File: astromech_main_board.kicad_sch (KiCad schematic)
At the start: 76 parts, among them IC1 MAX11645EUA+, J10 Conn_01x05, J11 Conn_01x06, J13 Conn_01x05, J14 Conn_01x04, J15 Conn_01x04, J18 Screw_Terminal_01x10, J19 Conn_01x04, J2 Conn_02x03_Odd_Even, J20 Conn_01x04, J21 Conn_01x04, J4 IO_XPAND, J5 Conn_01x06, J6 Conn_01x06, J8 Conn_01x03, J9 Conn_01x06, Q1 2N7002, U10 LS7366R, U11 LS7366R, U3 NCP1117-3.3_SOT223, U4 NCP1117-5.0_TO252, U5 SC16IS752IPW_128, U6 PCF8575PWR, U7 TCA9517ADGK, U8 74HC14, U9 LS7366R, Y1 8MHz, Y2 Crystal

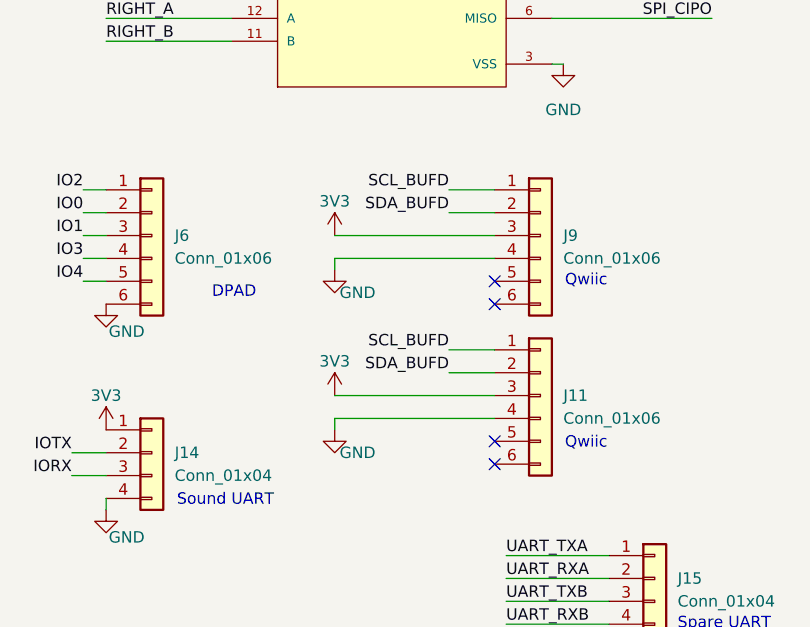
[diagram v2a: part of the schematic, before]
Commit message: switch qwiic pinout order
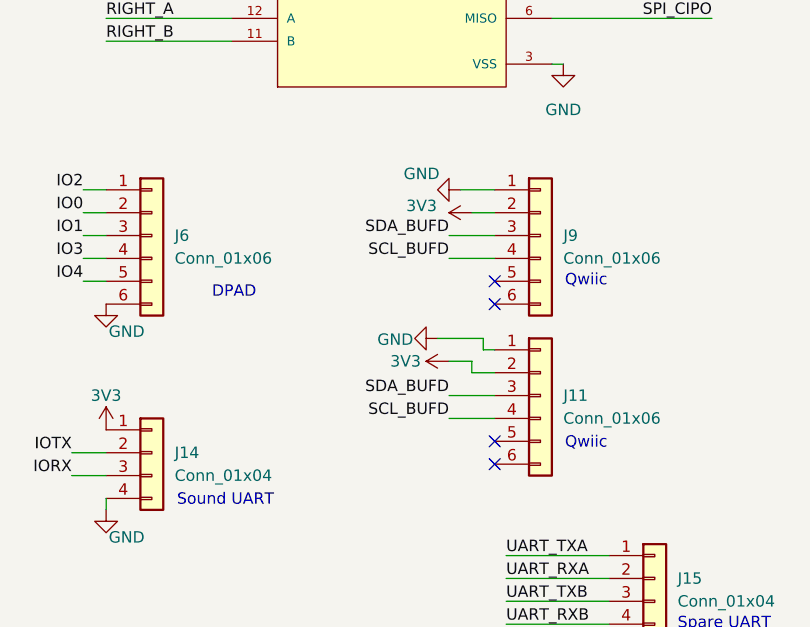
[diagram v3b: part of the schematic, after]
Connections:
- net 3V3: now also J11.2 (Pin_2), J9.2 (Pin_2); no longer J11.3 (Pin_3), J9.3 (Pin_3)
- net GND: now also J11.1 (Pin_1), J9.1 (Pin_1); no longer J11.4 (Pin_4), J9.4 (Pin_4)
- net SCL_BUFD: now also J11.4 (Pin_4), J9.4 (Pin_4); no longer J11.1 (Pin_1), J9.1 (Pin_1)
- net SDA_BUFD: now also J11.3 (Pin_3), J9.3 (Pin_3); no longer J11.2 (Pin_2), J9.2 (Pin_2)
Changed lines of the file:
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@@
 	(wire
 		(pts
-			(xy 257.81 182.88) (xy 252.73 182.88)
+			(xy 257.81 185.42) (xy 252.73 185.42)
 		)
 		(stroke
@@
 	(wire
 		(pts
+			(xy 252.73 203.2) (xy 257.81 203.2)
+		)
+		(stroke
+			(width 0)
+			(type default)
+		)
+	)
+	(wire
+		(pts
 			(xy -66.04 80.01) (xy -80.01 80.01)
 		)
@@
 	(wire
 		(pts
-			(xy 240.03 205.74) (xy 240.03 207.01)
+			(xy 251.46 196.85) (xy 256.54 196.85)
 		)
 		(stroke
@@
 		)
 	)
-	(wire
-		(pts
-			(xy 240.03 205.74) (xy 257.81 205.74)
-		)
-		(stroke
-			(width 0)
-			(type default)
-		)
-	)
 	(polyline
 		(pts
@@
 	(wire
 		(pts
-			(xy 252.73 198.12) (xy 257.81 198.12)
-		)
-		(stroke
-			(width 0)
-			(type default)
-		)
-	)
-	(wire
-		(pts
 			(xy 63.5 31.75) (xy 63.5 35.56)
 		)
@@
 		)
 	)
+	(wire
+		(pts
+			(xy 257.81 200.66) (xy 255.27 200.66)
+		)
+		(stroke
+			(width 0)
+			(type default)
+		)
+	)
 	(polyline
 		(pts
@@
 	(wire
 		(pts
-			(xy 240.03 187.96) (xy 257.81 187.96)
+			(xy 181.61 212.09) (xy 185.42 212.09)
 		)
 		(stroke
@@
 	(wire
 		(pts
-			(xy 181.61 212.09) (xy 185.42 212.09)
+			(xy 264.16 106.68) (xy 281.94 106.68)
 		)
 		(stroke
@@
 	(wire
 		(pts
-			(xy 264.16 106.68) (xy 281.94 106.68)
+			(xy 91.44 64.77) (xy 85.09 64.77)
 		)
 		(stroke
@@
 	(wire
 		(pts
-			(xy 91.44 64.77) (xy 85.09 64.77)
+			(xy 24.13 163.83) (xy 26.67 163.83)
 		)
 		(stroke
@@
 	(wire
 		(pts
-			(xy 24.13 163.83) (xy 26.67 163.83)
+			(xy 198.12 90.17) (xy 200.66 90.17)
 		)
 		(stroke
@@
 	(wire
 		(pts
-			(xy 198.12 90.17) (xy 200.66 90.17)
+			(xy 256.54 198.12) (xy 256.54 196.85)
 		)
 		(stroke
@@
 	(wire
 		(pts
-			(xy 252.73 200.66) (xy 257.81 200.66)
-		)
-		(stroke
-			(width 0)
-			(type default)
-		)
-	)
-	(wire
-		(pts
 			(xy 92.71 166.37) (xy 62.23 166.37)
 		)
@@
 	(wire
 		(pts
-			(xy 240.03 187.96) (xy 240.03 189.23)
+			(xy 254 180.34) (xy 257.81 180.34)
 		)
 		(stroke
@@
 	(wire
 		(pts
+			(xy 255.27 200.66) (xy 255.27 199.39)
+		)
+		(stroke
+			(width 0)
+			(type default)
+		)
+	)
+	(wire
+		(pts
 			(xy 83.82 267.97) (xy 90.17 267.97)
 		)
@@
 	(wire
 		(pts
-			(xy 257.81 180.34) (xy 252.73 180.34)
+			(xy 257.81 187.96) (xy 252.73 187.96)
 		)
 		(stroke
@@
 	(wire
 		(pts
-			(xy 240.03 203.2) (xy 257.81 203.2)
+			(xy 252.73 205.74) (xy 257.81 205.74)
 		)
 		(stroke
@@
 	(wire
 		(pts
+			(xy 255.27 182.88) (xy 257.81 182.88)
+		)
+		(stroke
+			(width 0)
+			(type default)
+		)
+	)
+	(wire
+		(pts
 			(xy 86.36 86.36) (xy 85.09 86.36)
 		)
@@
 	(wire
 		(pts
-			(xy 240.03 185.42) (xy 257.81 185.42)
-		)
-		(stroke
-			(width 0)
-			(type default)
-		)
-	)
-	(wire
-		(pts
 			(xy 100.33 27.94) (xy 100.33 30.48)
 		)
@@
 	(wire
 		(pts
+			(xy 257.81 198.12) (xy 256.54 198.12)
+		)
+		(stroke
+			(width 0)
+			(type default)
+		)
+	)
+	(wire
+		(pts
 			(xy 62.23 123.19) (xy 62.23 125.73)
 		)
@@
 	(wire
 		(pts
+			(xy 255.27 199.39) (xy 252.73 199.39)
+		)
+		(stroke
+			(width 0)
+			(type default)
+		)
+	)
+	(wire
+		(pts
 			(xy 180.34 146.05) (xy 203.2 146.05)
 		)
@@
 	)
 	(label "SDA_BUFD"
-		(at 252.73 200.66 180)
+		(at 252.73 203.2 180)
 		(effects
 			(font
@@
 	)
 	(label "SCL_BUFD"
-		(at 252.73 180.34 180)
+		(at 252.73 187.96 180)
 		(effects
 			(font
@@
 	)
 	(label "SCL_BUFD"
-		(at 252.73 198.12 180)
+		(at 252.73 205.74 180)
 		(effects
 			(font
@@
 	)
 	(label "SDA_BUFD"
-		(at 252.73 182.88 180)
+		(at 252.73 185.42 180)
 		(effects
 			(font
@@
 	(symbol
 		(lib_id "power:GND")
-		(at 240.03 207.01 0)
+		(at 251.46 196.85 270)
 		(unit 1)
 		(exclude_from_sim no)
@@
 		(dnp no)
 		(property "Reference" "#PWR076"
-			(at 240.03 213.36 0)
+			(at 245.11 196.85 0)
 			(effects
 				(font
@@
 		)
 		(property "Value" "GND"
-			(at 242.57 209.55 0)
+			(at 246.761 196.977 90)
 			(effects
 				(font
@@
 		)
 		(property "Footprint" ""
-			(at 240.03 207.01 0)
+			(at 251.46 196.85 0)
 			(effects
 				(font
@@
 		)
 		(property "Datasheet" ""
-			(at 240.03 207.01 0)
+			(at 251.46 196.85 0)
 			(effects
 				(font
@@
 		)
 		(property "Description" "Power symbol creates a global label with name \"GND\" , ground"
-			(at 240.03 207.01 0)
+			(at 251.46 196.85 0)
 			(effects
 				(font
@@
 	(symbol
 		(lib_id "power:GND")
-		(at 240.03 189.23 0)
+		(at 254 180.34 270)
 		(unit 1)
 		(exclude_from_sim no)
@@
 		(dnp no)
 		(property "Reference" "#PWR078"
-			(at 240.03 195.58 0)
+			(at 247.65 180.34 0)
 			(effects
 				(font
@@
 		)
 		(property "Value" "GND"
-			(at 242.57 191.77 0)
+			(at 249.682 178.562 90)
 			(effects
 				(font
@@
 		)
 		(property "Footprint" ""
-			(at 240.03 189.23 0)
+			(at 254 180.34 0)
 			(effects
 				(font
@@
 		)
 		(property "Datasheet" ""
-			(at 240.03 189.23 0)
+			(at 254 180.34 0)
 			(effects
 				(font
@@
 		)
 		(property "Description" "Power symbol creates a global label with name \"GND\" , ground"
-			(at 240.03 189.23 0)
+			(at 254 180.34 0)
 			(effects
 				(font
@@
 	(symbol
 		(lib_id "power:+3.3V")
-		(at 240.03 203.2 0)
+		(at 252.73 199.39 90)
 		(unit 1)
 		(exclude_from_sim no)
@@
 		(dnp no)
 		(property "Reference" "#PWR075"
-			(at 240.03 207.01 0)
+			(at 256.54 199.39 0)
 			(effects
 				(font
@@
 		)
 		(property "Value" "3V3"
-			(at 240.03 199.39 0)
+			(at 247.904 199.39 90)
 			(effects
 				(font
@@
 		)
 		(property "Footprint" ""
-			(at 240.03 203.2 0)
+			(at 252.73 199.39 0)
 			(effects
 				(font
@@
 		)
 		(property "Datasheet" ""
-			(at 240.03 203.2 0)
+			(at 252.73 199.39 0)
 			(effects
 				(font
@@
 		)
 		(property "Description" "Power symbol creates a global label with name \"+3.3V\""
-			(at 240.03 203.2 0)
+			(at 252.73 199.39 0)
 			(effects
 				(font
@@
 	(symbol
 		(lib_id "power:+3.3V")
-		(at 240.03 185.42 0)
+		(at 255.27 182.88 90)
 		(unit 1)
 		(exclude_from_sim no)
@@
 		(dnp no)
 		(property "Reference" "#PWR077"
-			(at 240.03 189.23 0)
+			(at 259.08 182.88 0)
 			(effects
 				(font
@@
 		)
 		(property "Value" "3V3"
-			(at 240.03 181.61 0)
+			(at 249.682 182.118 90)
 			(effects
 				(font
@@
 		)
 		(property "Footprint" ""
-			(at 240.03 185.42 0)
+			(at 255.27 182.88 0)
 			(effects
 				(font
@@
 		)
 		(property "Datasheet" ""
-			(at 240.03 185.42 0)
+			(at 255.27 182.88 0)
 			(effects
 				(font
@@
 		)
 		(property "Description" "Power symbol creates a global label with name \"+3.3V\""
-			(at 240.03 185.42 0)
+			(at 255.27 182.88 0)
 			(effects
 				(font

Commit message: schematic updates
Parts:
- removed J10, J13: Conn_01x05, astromech_footprints:691210910005, symbol Connector_Generic:Conn_01x05
- removed J14: Conn_01x04, astromech_footprints:691210910004, symbol Connector_Generic:Conn_01x04
- removed J5, J6: Conn_01x06, astromech_footprints:691210910006, symbol Connector_Generic:Conn_01x06
- added J1, J3, J7: Conn_01x03, astromech_footprints:691210910003, symbol Connector_Generic:Conn_01x03
- added J10: 61201621621, astromech_footprints:61201621621, symbol astromech_symbols:6120XX21621_61201621621
- added P15, P16, P17: TestPoint, TestPoint:TestPoint_Pad_D1.0mm, symbol Connector:TestPoint
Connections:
- net 3V3: now also J10.15
- net GND: now also J1.3 (Pin_3), J10.16, J3.3 (Pin_3), J7.3 (Pin_3)
- net IO0: now also J10.12
- net IO1: now also J10.10
- net IO2: now also J10.14
- net IO3: now also J10.8
- net IO38: now also J10.11
- net IO39: now also J10.9
- net IO4: now also J10.6
- net IO8: now also J4.14 (Pin_14); no longer J4.9 (Pin_9)
- net IORX: now also J7.2 (Pin_2)
- net IOTX: now also J7.1 (Pin_1)
- net SCL_BUFD: now also J1.1 (Pin_1), J3.1 (Pin_1)
- net SCR_SPICLK: now also J10.7
- net SCR_SPIQ: now also J10.13
- net SDA_BUFD: now also J1.2 (Pin_2), J3.2 (Pin_2)
- net at U6.13 (P10): now also J4.9 (Pin_9)
- net at U6.14 (P11): now also J4.10 (Pin_10)
- net at U6.15 (P12): now also J4.11 (Pin_11)
- net at U6.16 (P13): now also J4.12 (Pin_12)
- net at U6.17 (P14): now also J4.13 (Pin_13)
- net at U6.18 (P15): now also P15.1
- net at U6.19 (P16): now also P16.1
- net at U6.20 (P17): now also P17.1
- net IO10 renamed TOUCH_X+
- net TOUCH_X+: now also J10.3; no longer J4.10 (Pin_10)
- net IO17 renamed TOUCH_Y+
- net TOUCH_Y+: now also J10.4; no longer J4.11 (Pin_11)
- net IO19 renamed TOUCH_X-
- net TOUCH_X-: now also J10.1; no longer J4.12 (Pin_12)
- net IO21 renamed TOUCH_Y-
- net TOUCH_Y-: now also J10.2; no longer J4.13 (Pin_13)
- net IO35 renamed SCR_D/C
- net SCR_D/C: now also J10.5; no longer J4.14 (Pin_14)
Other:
- note added: "Screen data/command select"
- note added: "Touchscreen"
- moved on the sheet: J8

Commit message: new layout
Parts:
- removed P15, P16, P17: TestPoint, TestPoint:TestPoint_Pad_D1.0mm, symbol Connector:TestPoint
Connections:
- net +3.3V is gone; now on net 3V3: R8.1
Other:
- note added: "Screen/DPAD"
- note removed: "DPAD"
- note removed: "Screen"
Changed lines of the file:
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@@
 	(wire
 		(pts
-			(xy 62.23 186.69) (xy 63.5 186.69)
-		)
-		(stroke
-			(width 0)
-			(type default)
-		)
-	)
-	(wire
-		(pts
 			(xy 144.78 143.51) (xy 144.78 146.05)
 		)
@@
 	(wire
 		(pts
-			(xy 62.23 184.15) (xy 63.5 184.15)
-		)
-		(stroke
-			(width 0)
-			(type default)
-		)
-	)
-	(wire
-		(pts
 			(xy 273.05 93.98) (xy 274.32 93.98)
 		)
@@
 	(wire
 		(pts
-			(xy 63.5 181.61) (xy 62.23 181.61)
-		)
-		(stroke
-			(width 0)
-			(type default)
-		)
-	)
-	(wire
-		(pts
 			(xy 264.16 156.21) (xy 281.94 156.21)
 		)
@@
 		)
 	)
-	(text "DPAD"
-		(exclude_from_sim no)
-		(at 118.872 181.356 0)
-		(effects
-			(font
-				(size 1.27 1.27)
-			)
-		)
-	)
 	(text "Head Motor PWM"
 		(exclude_from_sim no)
@@
 		)
 	)
-	(text "Screen"
+	(text "Screen/DPAD"
 		(exclude_from_sim no)
-		(at 139.192 198.374 0)
+		(at 134.874 197.612 0)
 		(effects
 			(font
@@
 	)
 	(symbol
-		(lib_id "Connector:TestPoint")
-		(at 63.5 181.61 270)
-		(unit 1)
-		(exclude_from_sim no)
-		(in_bom yes)
-		(on_board yes)
-		(dnp no)
-		(property "Reference" "P15"
-			(at 69.85 181.61 90)
-			(effects
-				(font
-					(size 1.27 1.27)
-				)
-			)
-		)
-		(property "Value" "TestPoint"
-			(at 66.802 184.15 90)
-			(effects
-				(font
-					(size 1.27 1.27)
-				)
-				(hide yes)
-			)
-		)
-		(property "Footprint" "TestPoint:TestPoint_Pad_D1.0mm"
-			(at 63.5 186.69 0)
-			(effects
-				(font
-					(size 1.27 1.27)
-				)
-				(hide yes)
-			)
-		)
-		(property "Datasheet" "~"
-			(at 63.5 186.69 0)
-			(effects
-				(font
-					(size 1.27 1.27)
-				)
-				(hide yes)
-			)
-		)
-		(property "Description" "test point"
-			(at 63.5 181.61 0)
-			(effects
-				(font
-					(size 1.27 1.27)
-				)
-				(hide yes)
-			)
-		)
-		(pin "1"
-		)
-		(instances
-			(project "astromech_main_board"
-				(path "/3ed70c37-1dc6-4761-9813-fca49ce12494"
-					(reference "P15")
-					(unit 1)
-				)
-			)
-		)
-	)
-	(symbol
 		(lib_id "power:GND")
 		(at 191.77 92.71 0)
@@
 	)
 	(symbol
-		(lib_id "Connector:TestPoint")
-		(at 63.5 186.69 270)
-		(unit 1)
-		(exclude_from_sim no)
-		(in_bom yes)
-		(on_board yes)
-		(dnp no)
-		(property "Reference" "P17"
-			(at 69.85 186.69 90)
-			(effects
-				(font
-					(size 1.27 1.27)
-				)
-			)
-		)
-		(property "Value" "TestPoint"
-			(at 66.802 189.23 90)
-			(effects
-				(font
-					(size 1.27 1.27)
-				)
-				(hide yes)
-			)
-		)
-		(property "Footprint" "TestPoint:TestPoint_Pad_D1.0mm"
-			(at 63.5 191.77 0)
-			(effects
-				(font
-					(size 1.27 1.27)
-				)
-				(hide yes)
-			)
-		)
-		(property "Datasheet" "~"
-			(at 63.5 191.77 0)
-			(effects
-				(font
-					(size 1.27 1.27)
-				)
-				(hide yes)
-			)
-		)
-		(property "Description" "test point"
-			(at 63.5 186.69 0)
-			(effects
-				(font
-					(size 1.27 1.27)
-				)
-				(hide yes)
-			)
-		)
-		(pin "1"
-		)
-		(instances
-			(project "astromech_main_board"
-				(path "/3ed70c37-1dc6-4761-9813-fca49ce12494"
-					(reference "P17")
-					(unit 1)
-				)
-			)
-		)
-	)
-	(symbol
 		(lib_id "Connector_Generic:Conn_02x03_Odd_Even")
 		(at 187.96 181.61 0)
@@
 	)
 	(symbol
-		(lib_id "power:+3.3V")
-		(at 175.26 24.13 0)
-		(unit 1)
-		(exclude_from_sim no)
-		(in_bom yes)
-		(on_board yes)
-		(dnp no)
-		(fields_autoplaced yes)
-		(property "Reference" "#PWR09"
-			(at 175.26 27.94 0)
-			(effects
-				(font
-					(size 1.27 1.27)
-				)
-				(hide yes)
-			)
-		)
-		(property "Value" "+3.3V"
-			(at 175.26 19.05 0)
-			(effects
-				(font
-					(size 1.27 1.27)
-				)
-			)
-		)
-		(property "Footprint" ""
-			(at 175.26 24.13 0)
-			(effects
-				(font
-					(size 1.27 1.27)
-				)
-				(hide yes)
-			)
-		)
-		(property "Datasheet" ""
-			(at 175.26 24.13 0)
-			(effects
-				(font
-					(size 1.27 1.27)
-				)
-				(hide yes)
-			)
-		)
-		(property "Description" "Power symbol creates a global label with name \"+3.3V\""
-			(at 175.26 24.13 0)
-			(effects
-				(font
-					(size 1.27 1.27)
-				)
-				(hide yes)
-			)
-		)
-		(pin "1"
-		)
-		(instances
-			(project ""
-				(path "/3ed70c37-1dc6-4761-9813-fca49ce12494"
-					(reference "#PWR09")
-					(unit 1)
-				)
-			)
-		)
-	)
-	(symbol
 		(lib_id "Jumper:SolderJumper_3_Open")
 		(at 63.5 26.67 270)
@@
 	)
 	(symbol
-		(lib_id "Connector:TestPoint")
-		(at 63.5 184.15 270)
-		(unit 1)
-		(exclude_from_sim no)
-		(in_bom yes)
-		(on_board yes)
-		(dnp no)
-		(property "Reference" "P16"
-			(at 69.85 184.15 90)
-			(effects
-				(font
-					(size 1.27 1.27)
-				)
-			)
-		)
-		(property "Value" "TestPoint"
-			(at 66.802 186.69 90)
-			(effects
-				(font
-					(size 1.27 1.27)
-				)
-				(hide yes)
-			)
-		)
-		(property "Footprint" "TestPoint:TestPoint_Pad_D1.0mm"
-			(at 63.5 189.23 0)
-			(effects
-				(font
-					(size 1.27 1.27)
-				)
-				(hide yes)
-			)
-		)
-		(property "Datasheet" "~"
-			(at 63.5 189.23 0)
-			(effects
-				(font
-					(size 1.27 1.27)
-				)
-				(hide yes)
-			)
-		)
-		(property "Description" "test point"
-			(at 63.5 184.15 0)
-			(effects
-				(font
-					(size 1.27 1.27)
-				)
-				(hide yes)
-			)
-		)
-		(pin "1"
-		)
-		(instances
-			(project "astromech_main_board"
-				(path "/3ed70c37-1dc6-4761-9813-fca49ce12494"
-					(reference "P16")
-					(unit 1)
-				)
-			)
-		)
-	)
-	(symbol
 		(lib_id "power:+3.3V")
 		(at 24.13 66.04 270)
@@
 					(unit 1)
 				)
+			)
+		)
+	)
+	(symbol
+		(lib_id "power:+3.3V")
+		(at 175.26 24.13 0)
+		(unit 1)
+		(exclude_from_sim no)
+		(in_bom yes)
+		(on_board yes)
+		(dnp no)
+		(property "Reference" "#PWR014"
+			(at 175.26 27.94 0)
+			(effects
+				(font
+					(size 1.27 1.27)
+				)
+				(hide yes)
+			)
+		)
+		(property "Value" "3V3"
+			(at 175.26 20.32 0)
+			(effects
+				(font
+					(size 1.27 1.27)
+				)
+			)
+		)
+		(property "Footprint" ""
+			(at 175.26 24.13 0)
+			(effects
+				(font
+					(size 1.27 1.27)
+				)
+				(hide yes)
+			)
+		)
+		(property "Datasheet" ""
+			(at 175.26 24.13 0)
+			(effects
+				(font
+					(size 1.27 1.27)
+				)
+				(hide yes)
+			)
+		)
+		(property "Description" "Power symbol creates a global label with name \"+3.3V\""
+			(at 175.26 24.13 0)
+			(effects
+				(font
+					(size 1.27 1.27)
+				)
+				(hide yes)
+			)
+		)
+		(pin "1"
+		)
+		(instances
+			(project "astromech_main_board"
+				(path "/3ed70c37-1dc6-4761-9813-fca49ce12494"
+					(reference "#PWR014")
+					(unit 1)
+				)

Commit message: new layout done
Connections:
- net I2C_3V3_SCL: now also U13.8 (IO_15); no longer U13.9 (IO_16)
- net I2C_3V3_SDA: now also U13.9 (IO_16); no longer U13.8 (IO_15)
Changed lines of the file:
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@@
+		)
+	)
+	(label "I2C_3V3_SCL"
+		(at 77.47 241.3 0)
+		(fields_autoplaced yes)
+		(effects
+			(font
+				(size 1.27 1.27)
+			)
+			(justify left bottom)
 		)
 	)
@@
 		)
 	)
-	(label "I2C_3V3_SCL"
-		(at 77.47 245.11 0)
-		(fields_autoplaced yes)
-		(effects
-			(font
-				(size 1.27 1.27)
-			)
-			(justify left bottom)
-		)
-	)
 	(label "IO13"
 		(at 22.86 237.49 0)
@@
 		)
 	)
-	(label "I2C_3V3_SDA"
-		(at 77.47 241.3 0)
-		(fields_autoplaced yes)
-		(effects
-			(font
-				(size 1.27 1.27)
-			)
-			(justify left bottom)
-		)
-	)
 	(label "LEFT_A"
 		(at 214.63 233.68 180)
@@
 		)
 	)
+	(label "I2C_3V3_SDA"
+		(at 77.47 245.11 0)
+		(fields_autoplaced yes)
+		(effects
+			(font
+				(size 1.27 1.27)
+			)
+			(justify left bottom)
+		)
+	)
